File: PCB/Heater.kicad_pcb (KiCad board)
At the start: 2 copper layers, 51 parts, among them IC1 ATTINY45-P, J1 GND, J2 RST, P1 220V 50Hz, P2 CONN_01X04, P3 DS18B20, U1 MOC3023M

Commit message: A better packed version
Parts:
- removed D2: LED, Socket_Strips:Socket_Strip_Straight_1x02_Pitch2.54mm
- D1: footprint Diodes_SMD:Diode_Bridge_TO-269AA -> diodebridge:DIP-6_W7.62mm
- moved R38 61.3 mm to (127.6, 122.6), turned to 180 degrees
- moved R34 58.6 mm to (125.1, 122.6), turned to 0 degrees
- moved R36 57.1 mm to (127.6, 120.0), turned to 180 degrees
- moved R39 54.3 mm to (125.1, 120.0), turned to 0 degrees
- moved R37 53.2 mm to (127.6, 117.5), turned to 180 degrees
- moved R35 50.0 mm to (125.1, 117.5), turned to 0 degrees
- moved R33 49.4 mm to (127.6, 114.9), turned to 180 degrees
- moved R31 46.0 mm to (125.1, 114.9), turned to 0 degrees
- moved R30 45.9 mm to (127.6, 112.4), turned to 180 degrees
- moved R32 42.2 mm to (125.1, 112.4), turned to 0 degrees
- moved P1 33.0 mm to (124.5, 105.4), turned to 180 degrees
- moved P3 25.5 mm to (127.0, 85.1), turned to 270 degrees
- moved J1 19.8 mm to (127.0, 82.5)
- moved D3 19.3 mm to (106.7, 104.1), turned to 270 degrees
- moved C1 18.8 mm to (105.4, 90.2), turned to 180 degrees
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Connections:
- D1 pad 3: Net-(D1-Pad3) -> Net-(C1-Pad1)
- IC1 pad 2: Net-(IC1-Pad2) -> (no net)
- P1 pad 1: Net-(D1-Pad1) -> Net-(P1-Pad1)
- P1 pad 2: Net-(P1-Pad2) -> Net-(D1-Pad2)
- P3 pad 2: Net-(IC1-Pad2) -> Net-(IC1-Pad7)
- R1 pad 1: Net-(D1-Pad2) -> Net-(D1-Pad1)
- R1 pad 2: Net-(P1-Pad2) -> Net-(P1-Pad1)
- R10 pad 1: Net-(D1-Pad2) -> Net-(D1-Pad1)
- R10 pad 2: Net-(P1-Pad2) -> Net-(P1-Pad1)
- R11 pad 1: Net-(D1-Pad2) -> Net-(D1-Pad1)
- R11 pad 2: Net-(P1-Pad2) -> Net-(P1-Pad1)
- R12 pad 1: Net-(D1-Pad2) -> Net-(D1-Pad1)
- R12 pad 2: Net-(P1-Pad2) -> Net-(P1-Pad1)
- R13 pad 1: Net-(D1-Pad2) -> Net-(D1-Pad1)
- R13 pad 2: Net-(P1-Pad2) -> Net-(P1-Pad1)
- R14 pad 1: Net-(D1-Pad2) -> Net-(D1-Pad1)
- R14 pad 2: Net-(P1-Pad2) -> Net-(P1-Pad1)
- R15 pad 1: Net-(D1-Pad2) -> Net-(D1-Pad1)
- R15 pad 2: Net-(P1-Pad2) -> Net-(P1-Pad1)
- R16 pad 1: Net-(D1-Pad2) -> Net-(D1-Pad1)
- R16 pad 2: Net-(P1-Pad2) -> Net-(P1-Pad1)
- R17 pad 1: Net-(D1-Pad2) -> Net-(D1-Pad1)
- R17 pad 2: Net-(P1-Pad2) -> Net-(P1-Pad1)
- R18 pad 1: Net-(D1-Pad2) -> Net-(D1-Pad1)
- R18 pad 2: Net-(P1-Pad2) -> Net-(P1-Pad1)
- R19 pad 1: Net-(D1-Pad2) -> Net-(D1-Pad1)
- R19 pad 2: Net-(P1-Pad2) -> Net-(P1-Pad1)
- R2 pad 1: Net-(D1-Pad2) -> Net-(D1-Pad1)
- R2 pad 2: Net-(P1-Pad2) -> Net-(P1-Pad1)
- R20 pad 1: Net-(D1-Pad2) -> Net-(D1-Pad1)
- R20 pad 2: Net-(P1-Pad2) -> Net-(P1-Pad1)
- R21 pad 1: Net-(D1-Pad2) -> Net-(D1-Pad1)
- R21 pad 2: Net-(P1-Pad2) -> Net-(P1-Pad1)
- R22 pad 1: Net-(D1-Pad2) -> Net-(D1-Pad1)
- R22 pad 2: Net-(P1-Pad2) -> Net-(P1-Pad1)
- R23 pad 1: Net-(D1-Pad2) -> Net-(D1-Pad1)
- R23 pad 2: Net-(P1-Pad2) -> Net-(P1-Pad1)
- R24 pad 1: Net-(D1-Pad2) -> Net-(D1-Pad1)
- R24 pad 2: Net-(P1-Pad2) -> Net-(P1-Pad1)
- R25 pad 1: Net-(D1-Pad2) -> Net-(D1-Pad1)
- R25 pad 2: Net-(P1-Pad2) -> Net-(P1-Pad1)
- R27 pad 2: Net-(IC1-Pad7) -> Net-(IC1-Pad5)
- R28 pad 1: Net-(IC1-Pad2) -> Net-(IC1-Pad7)
- R3 pad 1: Net-(D1-Pad2) -> Net-(D1-Pad1)
- R3 pad 2: Net-(P1-Pad2) -> Net-(P1-Pad1)
- R30 pad 2: Net-(P1-Pad2) -> Net-(P1-Pad1)
- R31 pad 2: Net-(P1-Pad2) -> Net-(P1-Pad1)
- R32 pad 2: Net-(P1-Pad2) -> Net-(P1-Pad1)
- R33 pad 2: Net-(P1-Pad2) -> Net-(P1-Pad1)
- R34 pad 2: Net-(P1-Pad2) -> Net-(P1-Pad1)
- R35 pad 2: Net-(P1-Pad2) -> Net-(P1-Pad1)
- R36 pad 2: Net-(P1-Pad2) -> Net-(P1-Pad1)
- R37 pad 2: Net-(P1-Pad2) -> Net-(P1-Pad1)
- R38 pad 2: Net-(P1-Pad2) -> Net-(P1-Pad1)
- R39 pad 2: Net-(P1-Pad2) -> Net-(P1-Pad1)
- R4 pad 1: Net-(D1-Pad2) -> Net-(D1-Pad1)
- R4 pad 2: Net-(P1-Pad2) -> Net-(P1-Pad1)
- R5 pad 1: Net-(D1-Pad2) -> Net-(D1-Pad1)
- R5 pad 2: Net-(P1-Pad2) -> Net-(P1-Pad1)
- R6 pad 1: Net-(D1-Pad2) -> Net-(D1-Pad1)
- R6 pad 2: Net-(P1-Pad2) -> Net-(P1-Pad1)
- R7 pad 1: Net-(D1-Pad2) -> Net-(D1-Pad1)
- R7 pad 2: Net-(P1-Pad2) -> Net-(P1-Pad1)
- R8 pad 1: Net-(D1-Pad2) -> Net-(D1-Pad1)
- R8 pad 2: Net-(P1-Pad2) -> Net-(P1-Pad1)
- R9 pad 1: Net-(D1-Pad2) -> Net-(D1-Pad1)
- R9 pad 2: Net-(P1-Pad2) -> Net-(P1-Pad1)
- U1 pad 4: Net-(R30-Pad1) -> Net-(D1-Pad2)
- U1 pad 6: Net-(D1-Pad1) -> Net-(R30-Pad1)
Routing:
- net Net-(P1-Pad1): track 0.00 -> 108.9 mm
- net Net-(P1-Pad2): track 108.4 -> 0.00 mm
- net Net-(D1-Pad2): track 61.1 -> 7.62 mm
- net GNDREF: track 67.2 -> 110.9 mm
- net Net-(D1-Pad1): track 23.6 -> 67.1 mm
- net Net-(R30-Pad1): track 37.7 -> 56.3 mm
- net Net-(IC1-Pad2): track 13.3 -> 0.00 mm
- net Net-(C1-Pad1): track 57.2 -> 50.9 mm
- net Net-(IC1-Pad7): track 2.54 -> 8.26 mm
- net Net-(R29-Pad1): track 5.21 -> 7.94 mm
- net Net-(IC1-Pad5): track 2.54 -> 4.13 mm
- net Net-(D4-Pad2): track 0.00 -> 1.59 mm
- net Net-(D1-Pad3): track 1.57 -> 0.00 mm

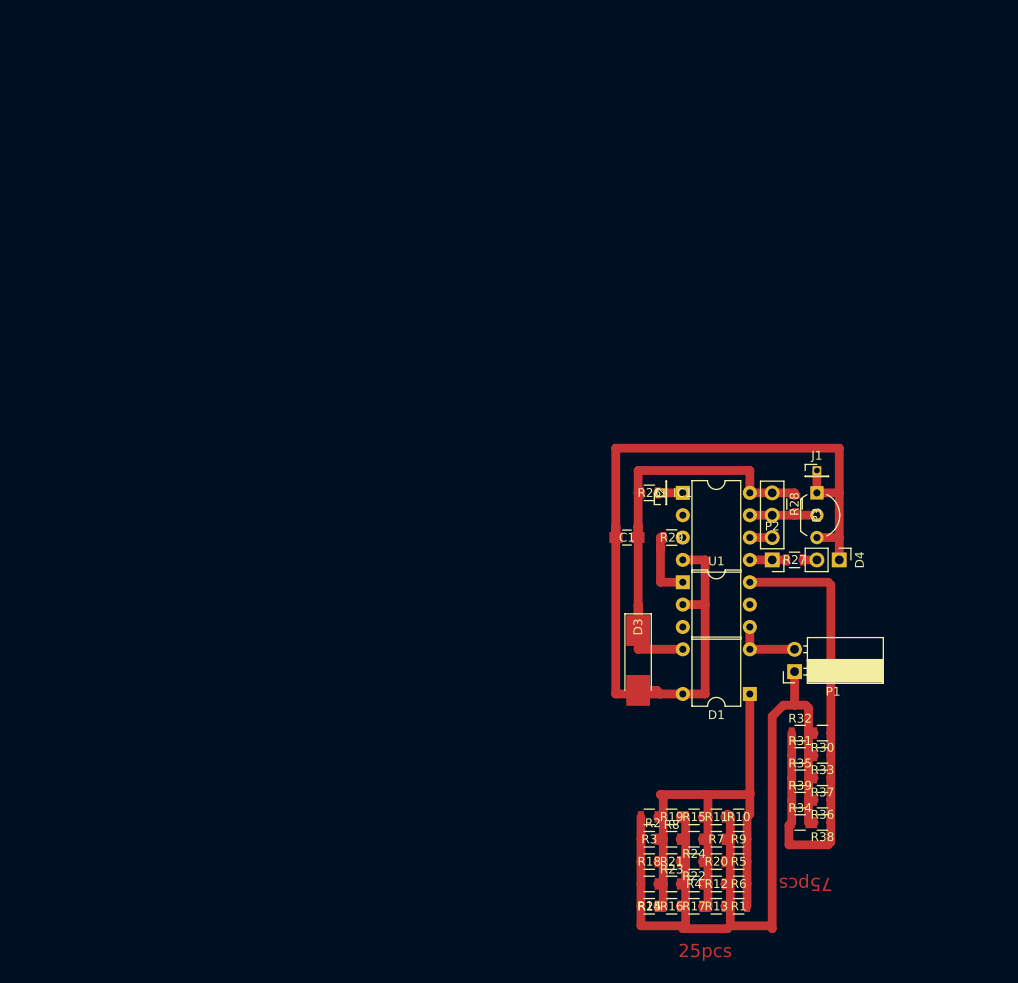
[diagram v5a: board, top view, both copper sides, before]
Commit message: new design with stronger resistors
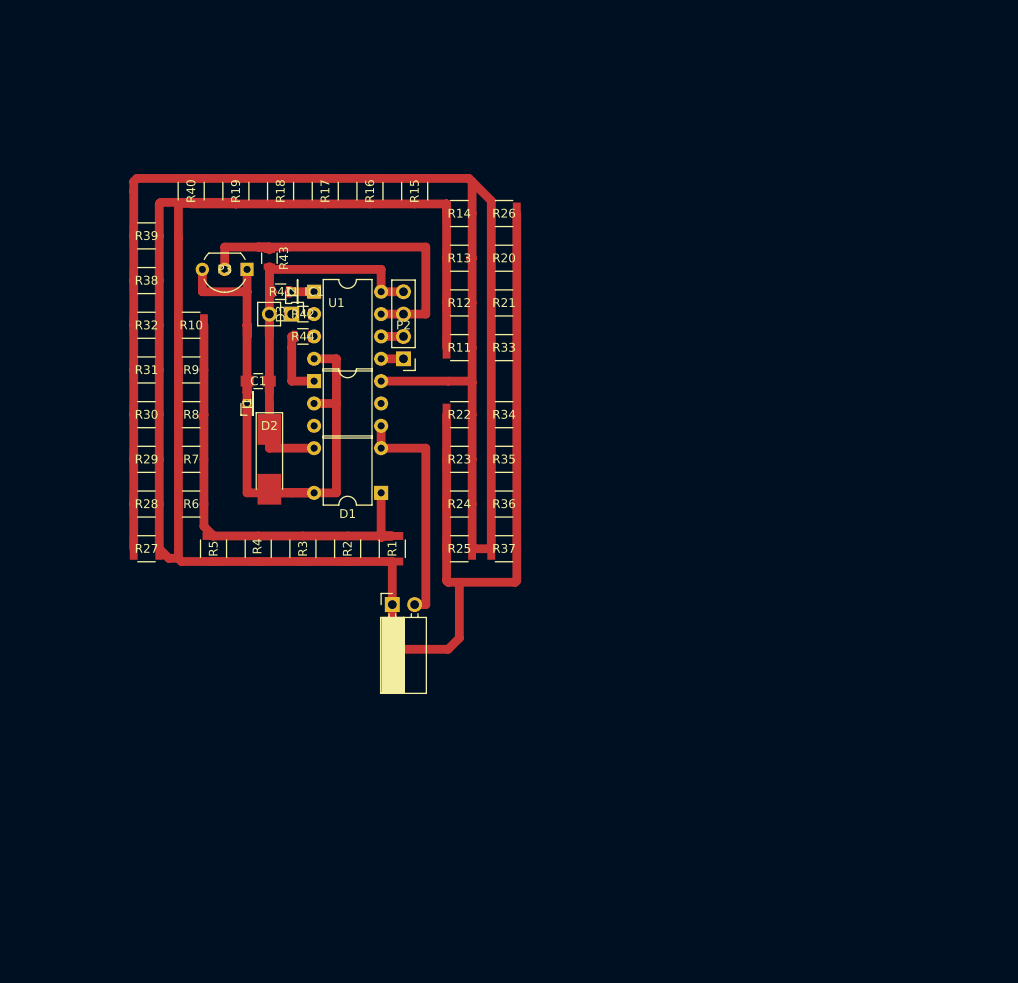
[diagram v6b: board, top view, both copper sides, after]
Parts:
- removed D4: LED, Socket_Strips:Socket_Strip_Straight_1x02_Pitch2.54mm
- added D2: ZD5V, Diodes_SMD:D_MELF_Handsoldering, F.Cu at (64.8, 81.3)
- added R40: 220K, Resistors_SMD:R_1210, F.Cu at (55.9, 50.8)
- added R41: 10K, Resistors_SMD:R_0805, F.Cu at (66.0, 62.2)
- added R42: 2K2, Resistors_SMD:R_0805, F.Cu at (68.6, 64.8)
- added R43: 5K, Resistors_SMD:R_0805, F.Cu at (64.8, 58.4)
- added R44: 470R, Resistors_SMD:R_0805, F.Cu at (68.6, 67.3)
- D3: value ZD5V -> LED; footprint Diodes_SMD:D_MELF_Handsoldering -> Socket_Strips:Socket_Strip_Straight_1x02_Pitch2.54mm
- R1, R10, R11, R12, R13, R14, R15, R16, R17, R18, R19, R2, R20, R21, R22, R23, R24, R25, R3, R30, R31, R32, R33, R34, R35, R36, R37, R38, R39, R4, R5, R6, R7, R8, R9: value 560K -> 220K; footprint Resistors_SMD:R_0805 -> Resistors_SMD:R_1210
- R26: value 10K -> 220K; footprint Resistors_SMD:R_0805 -> Resistors_SMD:R_1210
- R27: value 2K2 -> 220K; footprint Resistors_SMD:R_0805 -> Resistors_SMD:R_1210
- R28: value 5K -> 220K; footprint Resistors_SMD:R_0805 -> Resistors_SMD:R_1210
- R29: value 470R -> 220K; footprint Resistors_SMD:R_0805 -> Resistors_SMD:R_1210
- moved R38 98.5 mm to (50.8, 61.0), turned to 0 degrees
- moved R39 98.1 mm to (50.8, 55.9)
- moved R17 91.4 mm to (71.1, 50.8), turned to 270 degrees
- moved R16 88.2 mm to (76.2, 50.8), turned to 270 degrees
- moved R32 87.6 mm to (50.8, 66.0)
- moved R18 87.0 mm to (66.0, 50.8), turned to 270 degrees
- moved R19 86.7 mm to (61.0, 50.8), turned to 270 degrees
- moved R31 86.3 mm to (50.8, 71.1)
- moved R30 84.9 mm to (50.8, 76.2), turned to 0 degrees
- moved R10 83.6 mm to (55.9, 66.0)
- moved R9 82.0 mm to (55.9, 71.1)
- moved R14 81.6 mm to (86.4, 53.3)
- moved R13 79.2 mm to (86.4, 58.4), turned to 180 degrees
- moved R15 77.9 mm to (81.3, 50.8), turned to 270 degrees
- moved R6 75.7 mm to (55.9, 86.4)
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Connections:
- D3 pad 1: Net-(C1-Pad1) -> Net-(D3-Pad1)
- D3 pad 2: GNDREF -> Net-(C1-Pad1)
- IC1 pad 2: (no net) -> Net-(IC1-Pad2)
- R11 pad 1: Net-(D1-Pad1) -> Net-(R11-Pad1)
- R12 pad 1: Net-(D1-Pad1) -> Net-(R11-Pad1)
- R13 pad 1: Net-(D1-Pad1) -> Net-(R11-Pad1)
- R14 pad 1: Net-(D1-Pad1) -> Net-(R11-Pad1)
- R15 pad 1: Net-(D1-Pad1) -> Net-(R11-Pad1)
- R16 pad 1: Net-(D1-Pad1) -> Net-(R11-Pad1)
- R17 pad 1: Net-(D1-Pad1) -> Net-(R11-Pad1)
- R18 pad 1: Net-(D1-Pad1) -> Net-(R11-Pad1)
- R19 pad 1: Net-(D1-Pad1) -> Net-(R11-Pad1)
- R20 pad 1: Net-(D1-Pad1) -> Net-(R11-Pad1)
- R21 pad 1: Net-(D1-Pad1) -> Net-(R11-Pad1)
- R22 pad 1: Net-(D1-Pad1) -> Net-(R11-Pad1)
- R23 pad 1: Net-(D1-Pad1) -> Net-(R11-Pad1)
- R24 pad 1: Net-(D1-Pad1) -> Net-(R11-Pad1)
- R25 pad 1: Net-(D1-Pad1) -> Net-(R11-Pad1)
- R26 pad 1: Net-(IC1-Pad1) -> Net-(R11-Pad1)
- R26 pad 2: Net-(C1-Pad1) -> Net-(P1-Pad1)
- R27 pad 1: Net-(D4-Pad2) -> Net-(R11-Pad1)
- R27 pad 2: Net-(IC1-Pad5) -> Net-(P1-Pad1)
- R28 pad 1: Net-(IC1-Pad7) -> Net-(R11-Pad1)
- R28 pad 2: Net-(C1-Pad1) -> Net-(P1-Pad1)
- R29 pad 1: Net-(R29-Pad1) -> Net-(R11-Pad1)
- R29 pad 2: Net-(IC1-Pad3) -> Net-(P1-Pad1)
- R30 pad 1: Net-(R30-Pad1) -> Net-(R11-Pad1)
- R31 pad 1: Net-(R30-Pad1) -> Net-(R11-Pad1)
- R32 pad 1: Net-(R30-Pad1) -> Net-(R11-Pad1)
- R33 pad 1: Net-(R30-Pad1) -> Net-(R11-Pad1)
- R34 pad 1: Net-(R30-Pad1) -> Net-(R11-Pad1)
- R35 pad 1: Net-(R30-Pad1) -> Net-(R11-Pad1)
- R36 pad 1: Net-(R30-Pad1) -> Net-(R11-Pad1)
- R37 pad 1: Net-(R30-Pad1) -> Net-(R11-Pad1)
- R38 pad 1: Net-(R30-Pad1) -> Net-(R11-Pad1)
- R39 pad 1: Net-(R30-Pad1) -> Net-(R11-Pad1)
- U1 pad 1: Net-(R29-Pad1) -> Net-(R44-Pad1)
- U1 pad 6: Net-(R30-Pad1) -> Net-(R11-Pad1)
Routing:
- net Net-(R11-Pad1): track 0.00 -> 177.8 mm
- net Net-(P1-Pad1): track 108.9 -> 255.3 mm
- net Net-(R30-Pad1): track 56.3 -> 0.00 mm
- net GNDREF: track 110.9 -> 72.6 mm
- net Net-(IC1-Pad7): track 8.26 -> 39.7 mm
- net Net-(D1-Pad2): track 7.62 -> 26.7 mm
- net Net-(D1-Pad1): track 67.1 -> 51.7 mm
- net Net-(R29-Pad1): track 7.94 -> 0.00 mm
- net Net-(R44-Pad1): track 0.00 -> 7.94 mm
- net Net-(IC1-Pad5): track 4.13 -> 2.54 mm
- net Net-(D4-Pad2): track 1.59 -> 0.00 mm
- net Net-(C1-Pad1): track 50.9 -> 52.2 mm
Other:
- board text removed: "25pcs"
- board text removed: "75pcs"

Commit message: Possible layout
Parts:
- moved R6 55.7 mm to (105.4, 61.0), turned to 0 degrees
- moved R13 53.6 mm to (58.4, 104.1), turned to 90 degrees
- moved R8 49.7 mm to (105.4, 80.0), turned to 270 degrees
- moved R12 48.4 mm to (67.3, 108.0), turned to 90 degrees
- moved R25 48.4 mm to (39.4, 80.0), turned to 0 degrees
- moved R7 47.9 mm to (81.3, 40.6), turned to 90 degrees
- moved R5 47.1 mm to (62.2, 44.5), turned to 90 degrees
- moved R9 46.2 mm to (95.2, 95.2), turned to 0 degrees
- moved R10 43.7 mm to (95.2, 47.0), turned to 90 degrees
- moved R24 42.4 mm to (44.5, 92.7), turned to 0 degrees
- moved R4 36.9 mm to (47.0, 58.4), turned to 180 degrees
- moved R11 35.8 mm to (96.5, 102.9), turned to 90 degrees
- moved R27 31.0 mm to (76.2, 109.2), turned to 90 degrees
- moved R22 30.5 mm to (87.6, 106.7), turned to 90 degrees
- moved R3 27.5 mm to (45.7, 76.2), turned to 180 degrees
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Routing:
- net Net-(D1-Pad1): track 51.7 -> 188.9 mm
- net Net-(R11-Pad1): track 177.8 -> 297.3 mm
- net Net-(P1-Pad1): track 255.3 -> 301.5 mm
- net Net-(D1-Pad2): track 26.7 -> 21.6 mm
